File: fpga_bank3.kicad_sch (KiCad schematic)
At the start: 1 part, among them U2 XC7A50T-FGG484

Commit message: Schematic finished, starting layout
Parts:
- added C79, C80, C81, C82, C83, C84, C86, C87, C88, C89, C90, C91: 100n, Capacitor_SMD:C_0402_1005Metric_Pad0.74x0.62mm_HandSolder, symbol Device:C_Small
- added C85, C92: 4.7u, Capacitor_SMD:C_0402_1005Metric_Pad0.74x0.62mm_HandSolder, symbol Device:C_Small
- added R33: 3.9k, Resistor_SMD:R_0402_1005Metric_Pad0.72x0.64mm_HandSolder, symbol Device:R_Small
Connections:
- net +3V3: now also C79.2, C80.2, C81.2, C82.2, C83.2, C84.2, C85.2, C86.2, C87.2, C88.2, C89.2, C90.2, C91.2, C92.2
- net PI_UART_TX: now reaches U2.B1 (IO_L1P_T0_AD4P_35)
- net PI_UART_RX: now reaches U2.C2 (IO_L2P_T0_AD12P_35)
- net PCIE_DET_WAKE: now reaches U2.E2 (IO_L4P_T0_35)
- net at U2.F3 (IO_L6P_T0_35): now also R33.1
- net PCIE_CLKREQ_N: now reaches U2.G1 (IO_L5P_T0_AD13P_35)
- net SPI1_SCK: now reaches U2.G4 (IO_L12N_T1_MRCC_35)
- net REFCLK: now reaches U2.H4 (IO_L12P_T1_MRCC_35)
- net PCIE_RST_B: now reaches U2.J1 (IO_L7N_T1_AD6N_35)
- net SPI1_MOSI: now reaches U2.J4 (IO_L13N_T2_MRCC_35)
- net PI_GPIO13: now reaches U2.J6 (IO_L17N_T2_35)
- net SPI1_CE1: now reaches U2.K3 (IO_L14N_T2_SRCC_35)
- net SPI1_MISO: now reaches U2.K4 (IO_L13P_T2_MRCC_35)
- net PI_GPIO12: now reaches U2.K6 (IO_L17P_T2_35)
- net PI_GPIO4: now reaches U2.L1 (IO_L15N_T2_DQS_35)
- net SPI1_CE0: now reaches U2.L3 (IO_L14P_T2_SRCC_35)
- net PI_GPIO26: now reaches U2.L4 (IO_L18N_T2_35)
- net PI_GPIO22: now reaches U2.L5 (IO_L18P_T2_35)
- net SPI1_CE2: now reaches U2.M1 (IO_L15P_T2_DQS_35)
- net PI_GPIO6: now reaches U2.M2 (IO_L16N_T2_35)
- net PI_GPIO5: now reaches U2.M3 (IO_L16P_T2_35)
- net PI_GPIO27: now reaches U2.N4 (IO_L19P_T3_35)
- new net GND: C79.1, C80.1, C81.1, C82.1, C83.1, C84.1, C85.1, C86.1, C87.1, C88.1, C89.1, C90.1, C91.1, C92.1
- new net PCIE_PWR_EN: R33.2
- no-connect marks 0 -> 79
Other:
- note added: "-->"
- note added: "<--"
- title: FPGA Bank 34 & 35 -> FPGA Power
- moved on the sheet: U2C

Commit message: Updated titleblock texts
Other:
- title: FPGA Power -> FPGA Banks 34 & 35
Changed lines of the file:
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@@
   (paper "A4")
   (title_block
-    (title "FPGA Power")
-    (date "2024-02-11")
+    (title "FPGA Banks 34 & 35")
+    (date "2024-02-14")
     (rev "0.1")
     (company "George Smart, M1GEO")

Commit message: Started routing. More to go
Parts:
- removed R33: 3.9k, Resistor_SMD:R_0402_1005Metric_Pad0.72x0.64mm_HandSolder, symbol Device:R_Small
- added R17: 3.9k, Resistor_SMD:R_0402_1005Metric_Pad0.72x0.64mm_HandSolder, symbol Device:R_Small
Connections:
- net PCIE_CLKREQ_N: now also U2.J1 (IO_L7N_T1_AD6N_35); no longer U2.G1 (IO_L5P_T0_AD13P_35)
- net PCIE_DET_WAKE: now also U2.K1 (IO_L7P_T1_AD6P_35); no longer U2.E2 (IO_L4P_T0_35)
- net PCIE_PWR_EN: now also R17.2
- net PCIE_RST_B: now also U2.G1 (IO_L5P_T0_AD13P_35); no longer U2.J1 (IO_L7N_T1_AD6N_35)
- net PI_GPIO22: now also U2.F3 (IO_L6P_T0_35); no longer U2.L5 (IO_L18P_T2_35)
- net PI_GPIO27: now also U2.B2 (IO_L2N_T0_AD12N_35); no longer U2.N4 (IO_L19P_T3_35)
- net PI_GPIO4: now also U2.F1 (IO_L5N_T0_AD13N_35); no longer U2.L1 (IO_L15N_T2_DQS_35)
- net PI_UART_RX: now also U2.E1 (IO_L3P_T0_DQS_AD5P_35); no longer U2.C2 (IO_L2P_T0_AD12P_35)
- net PI_UART_TX: now also U2.L1 (IO_L15N_T2_DQS_35); no longer U2.B1 (IO_L1P_T0_AD4P_35)
- net PI_GPIO17: now reaches U2.D1 (IO_L3N_T0_DQS_AD5N_35)
- net PI_GPIO2: now reaches U2.P1 (IO_L20N_T3_35)
- net at U2.R1 (IO_L20P_T3_35): now also R17.1
- net PI_GPIO12: no longer names the net of U2.K6 (IO_L17P_T2_35)
- net PI_GPIO13: no longer names the net of U2.J6 (IO_L17N_T2_35)
- net PI_GPIO26: no longer names the net of U2.L4 (IO_L18N_T2_35)
- net PI_GPIO5: no longer names the net of U2.M3 (IO_L16P_T2_35)
- net PI_GPIO6: no longer names the net of U2.M2 (IO_L16N_T2_35)
- net REFCLK: no longer names the net of U2.H4 (IO_L12P_T1_MRCC_35)
- net SPI1_CE0: no longer names the net of U2.L3 (IO_L14P_T2_SRCC_35)
- net SPI1_CE1: no longer names the net of U2.K3 (IO_L14N_T2_SRCC_35)
- net SPI1_CE2 renamed PI_GPIO3
- net SPI1_MISO: no longer names the net of U2.K4 (IO_L13P_T2_MRCC_35)
- net SPI1_MOSI: no longer names the net of U2.J4 (IO_L13N_T2_MRCC_35)
- net SPI1_SCK: no longer names the net of U2.G4 (IO_L12N_T1_MRCC_35)
- new net PI_GPIO18: U2.B1 (IO_L1P_T0_AD4P_35)
- no-connect marks 79 -> 84
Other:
- moved on the sheet: C79, C80, C81, C82, C83, C84, C85, C86, C87, C88, C89, C90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

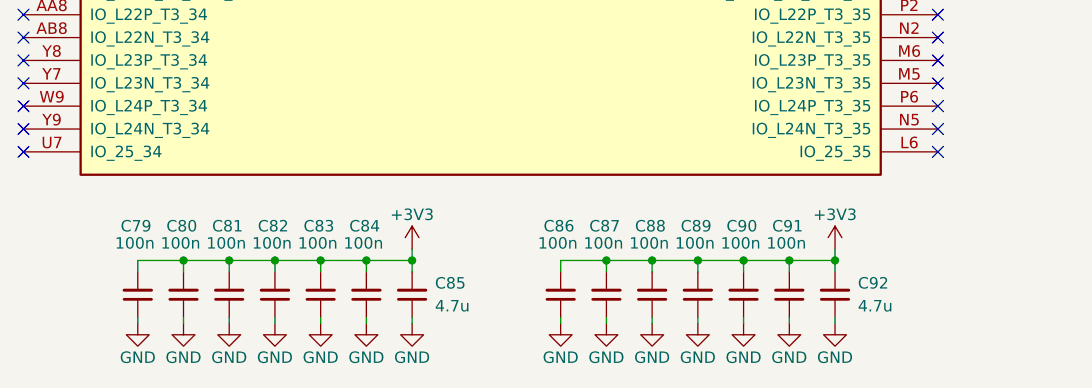
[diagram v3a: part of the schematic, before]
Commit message: Updated decoupling. Need to work out larger planes and fills.
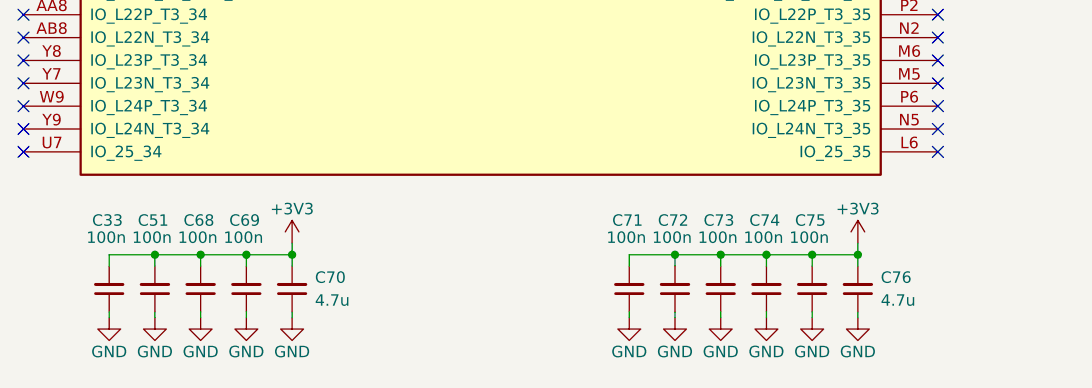
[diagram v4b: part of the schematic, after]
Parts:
- removed C79, C80, C81, C82, C83, C84, C86, C87, C88, C89, C90, C91: 100n, Capacitor_SMD:C_0402_1005Metric_Pad0.74x0.62mm_HandSolder, symbol Device:C_Small
- removed C85, C92: 4.7u, Capacitor_SMD:C_0402_1005Metric_Pad0.74x0.62mm_HandSolder, symbol Device:C_Small
- added C33, C51, C68, C69, C71, C72, C73, C74, C75: 100n, Capacitor_SMD:C_0402_1005Metric_Pad0.74x0.62mm_HandSolder, symbol Device:C_Small
- added C70, C76: 4.7u, Capacitor_SMD:C_0402_1005Metric_Pad0.74x0.62mm_HandSolder, symbol Device:C_Small
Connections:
- net +3V3: now also C33.2, C51.2, C68.2, C69.2, C70.2, C71.2, C72.2, C73.2, C74.2, C75.2, C76.2
- net GND: now also C33.1, C51.1, C68.1, C69.1, C70.1, C71.1, C72.1, C73.1, C74.1, C75.1, C76.1

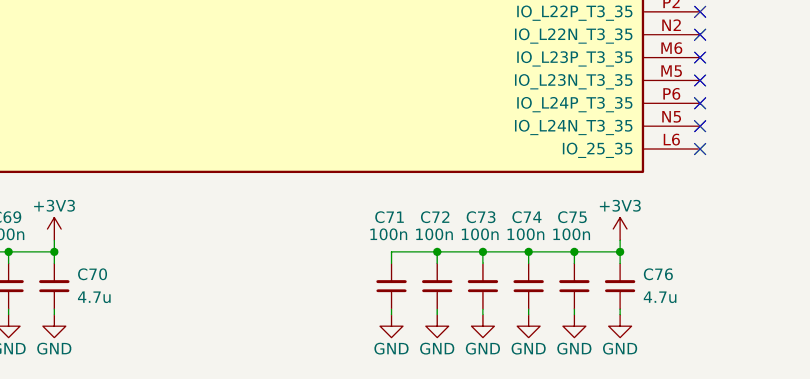
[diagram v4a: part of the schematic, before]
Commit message: Routing finished; Need to battle through the DRCs now. There's a few!
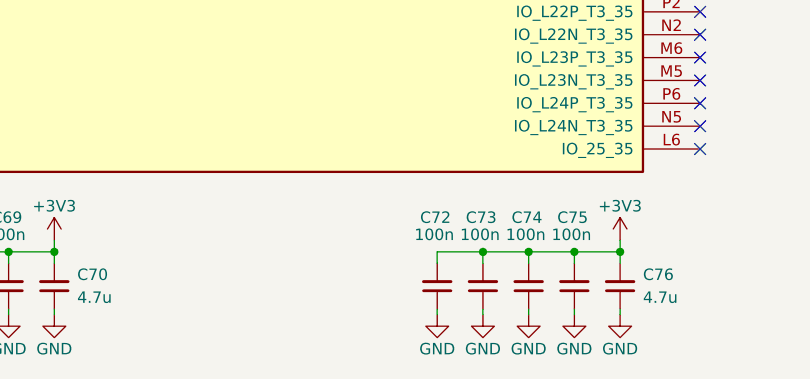
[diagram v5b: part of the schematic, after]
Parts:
- removed C71: 100n, Capacitor_SMD:C_0402_1005Metric_Pad0.74x0.62mm_HandSolder, symbol Device:C_Small
- R17: footprint Resistor_SMD:R_0402_1005Metric_Pad0.72x0.64mm_HandSolder -> Resistor_SMD:R_0402_1005Metric
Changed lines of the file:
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@@
   (junction (at 87.63 181.61) (diameter 0) (color 0 0 0 0)
-  )
-  (junction (at 135.255 181.61) (diameter 0) (color 0 0 0 0)
   )
   (junction (at 154.305 22.86) (diameter 0) (color 0 0 0 0)
@@
     (stroke (width 0) (type default))
   )
-  (wire (pts (xy 130.175 187.96) (xy 130.175 188.595))
-    (stroke (width 0) (type default))
-  )
   (wire (pts (xy 140.335 187.96) (xy 140.335 188.595))
     (stroke (width 0) (type default))
@@
     (stroke (width 0) (type default))
   )
-  (wire (pts (xy 130.175 181.61) (xy 135.255 181.61))
-    (stroke (width 0) (type default))
-  )
   (wire (pts (xy 80.645 25.4) (xy 80.645 22.86))
     (stroke (width 0) (type default))
@@
   )
   (wire (pts (xy 141.605 22.86) (xy 141.605 25.4))
-    (stroke (width 0) (type default))
-  )
-  (wire (pts (xy 130.175 182.88) (xy 130.175 181.61))
     (stroke (width 0) (type default))
   )
@@
       (effects (font (size 1.27 1.27)))
     )
-    (property "Footprint" "Resistor_SMD:R_0402_1005Metric_Pad0.72x0.64mm_HandSolder" (at 170.815 144.78 0)
+    (property "Footprint" "Resistor_SMD:R_0402_1005Metric" (at 170.815 144.78 0)
       (effects (font (size 1.27 1.27)) hide)
     )
@@
     )
   )
-  (symbol (lib_id "Device:C_Small") (at 130.175 185.42 180) (unit 1)
-    (in_bom yes) (on_board yes) (dnp no)
-    (property "Reference" "C71" (at 128.27 177.8 0)
-      (effects (font (size 1.27 1.27)) (justify right))
-    )
-    (property "Value" "100n" (at 127.635 179.705 0)
-      (effects (font (size 1.27 1.27)) (justify right))
-    )
-    (property "Footprint" "Capacitor_SMD:C_0402_1005Metric_Pad0.74x0.62mm_HandSolder" (at 130.175 185.42 0)
-      (effects (font (size 1.27 1.27)) hide)
-    )
-    (property "Datasheet" "https://datasheet.lcsc.com/lcsc/2304140030_Samsung-Electro-Mechanics-CL05B104KO5NNNC_C1525.pdf" (at 130.175 185.42 0)
-      (effects (font (size 1.27 1.27)) hide)
-    )
-    (property "LCSC" "C1525" (at 130.175 185.42 90)
-      (effects (font (size 1.27 1.27)) hide)
-    )
-    (pin "2")
-    (pin "1")
-    (instances
-      (project "Pi5-Artix50T-Hat"
-        (path "/e63e39d7-6ac0-4ffd-8aa3-1841a4541b55/58f29d61-b732-4149-afb6-3ea37966fd1b/478e6a6c-f816-4e6b-8386-2aa7bc333436"
-          (reference "C71") (unit 1)
-        )
-      )
-    )
-  )
   (symbol (lib_id "power:GND") (at 92.71 188.595 0) (unit 1)
     (in_bom yes) (on_board yes) (dnp no)
@@
         )
       )
-    )
-  )
-  (symbol (lib_id "power:GND") (at 130.175 188.595 0) (unit 1)
-    (in_bom yes) (on_board yes) (dnp no)
-    (property "Reference" "#PWR0115" (at 130.175 194.945 0)
-      (effects (font (size 1.27 1.27)) hide)
-    )
-    (property "Value" "GND" (at 130.175 192.405 0)
-      (effects (font (size 1.27 1.27)))
-    )
-    (property "Footprint" "" (at 130.175 188.595 0)
-      (effects (font (size 1.27 1.27)) hide)
-    )
-    (property "Datasheet" "" (at 130.175 188.595 0)
-      (effects (font (size 1.27 1.27)) hide)
-    )
-    (pin "1")
-    (instances
-      (project "Pi5-Artix50T-Hat"
-        (path "/e63e39d7-6ac0-4ffd-8aa3-1841a4541b55/58f29d61-b732-4149-afb6-3ea37966fd1b/478e6a6c-f816-4e6b-8386-2aa7bc333436"
-          (reference "#PWR0115") (unit 1)
-        )
-      )

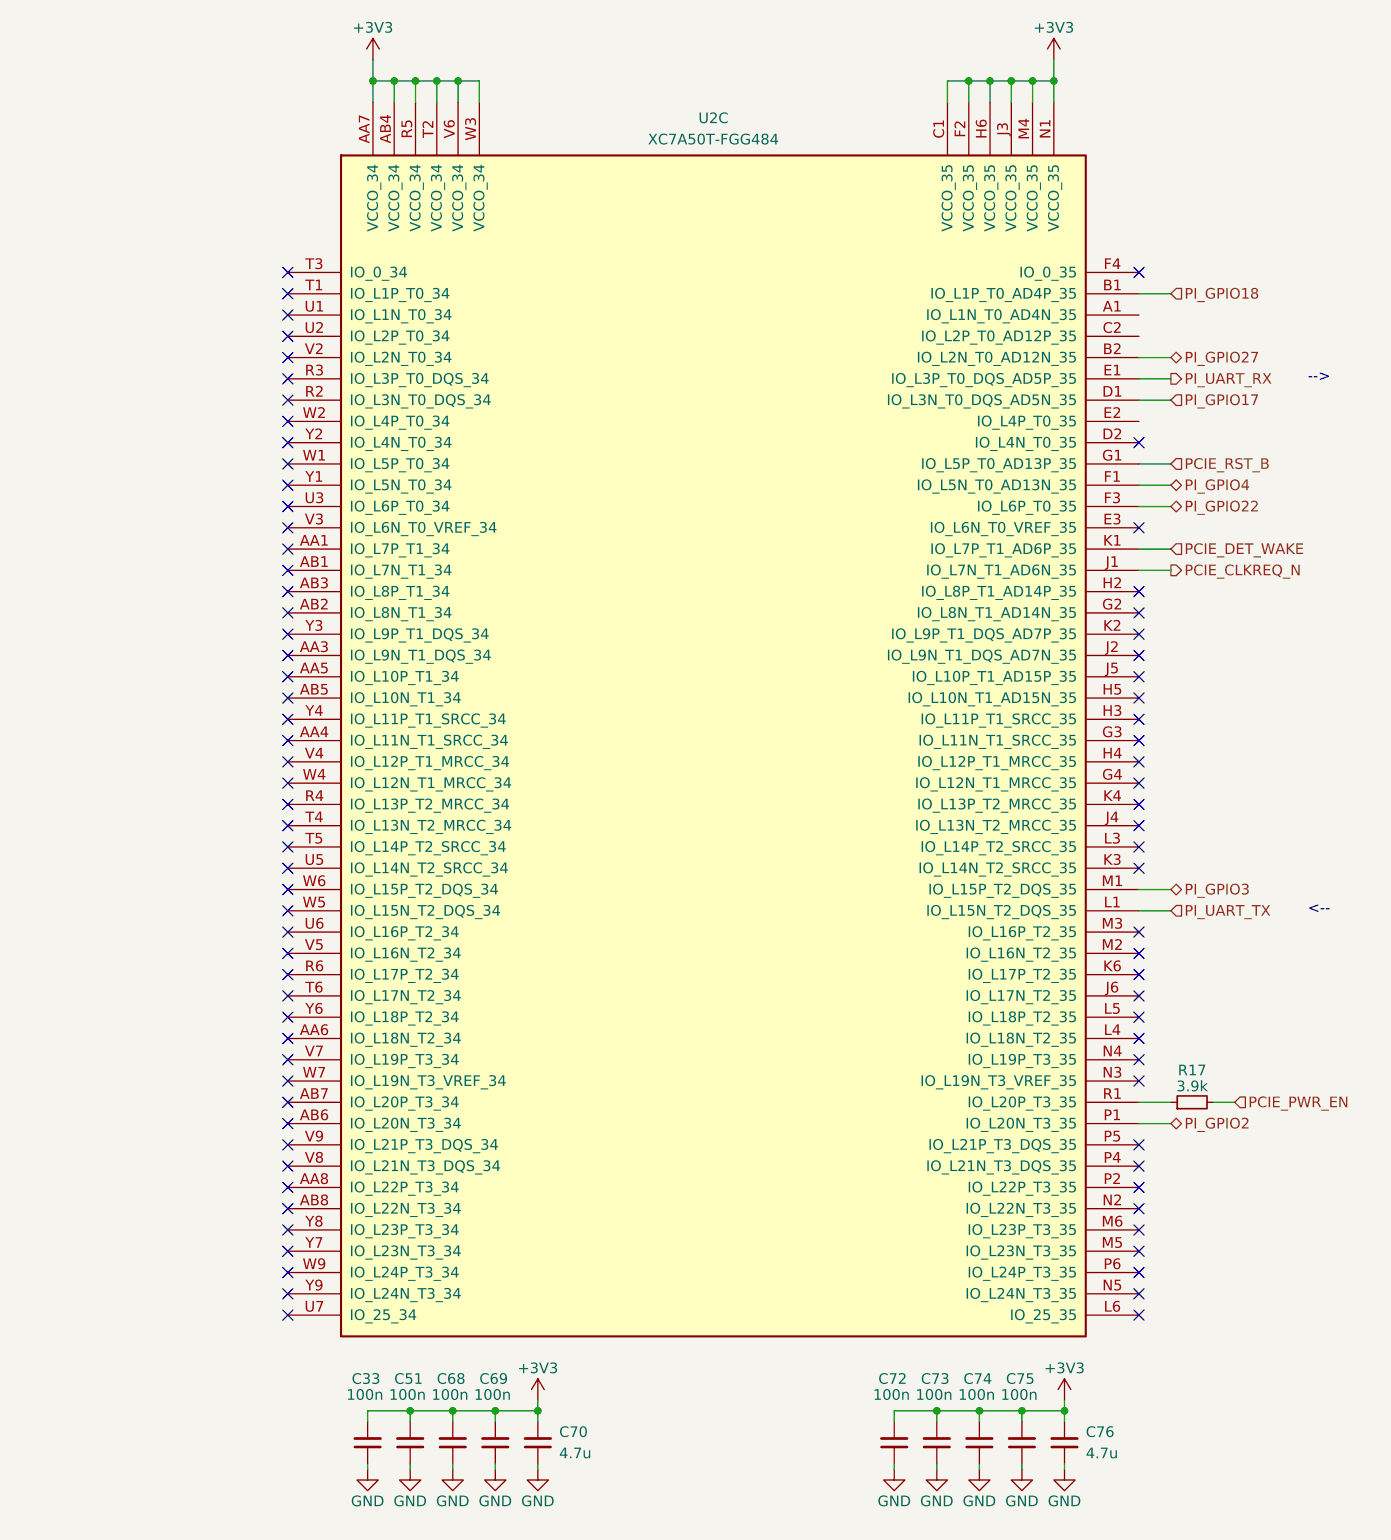
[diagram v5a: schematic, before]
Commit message: Ordered boards from JLCPCB for V1
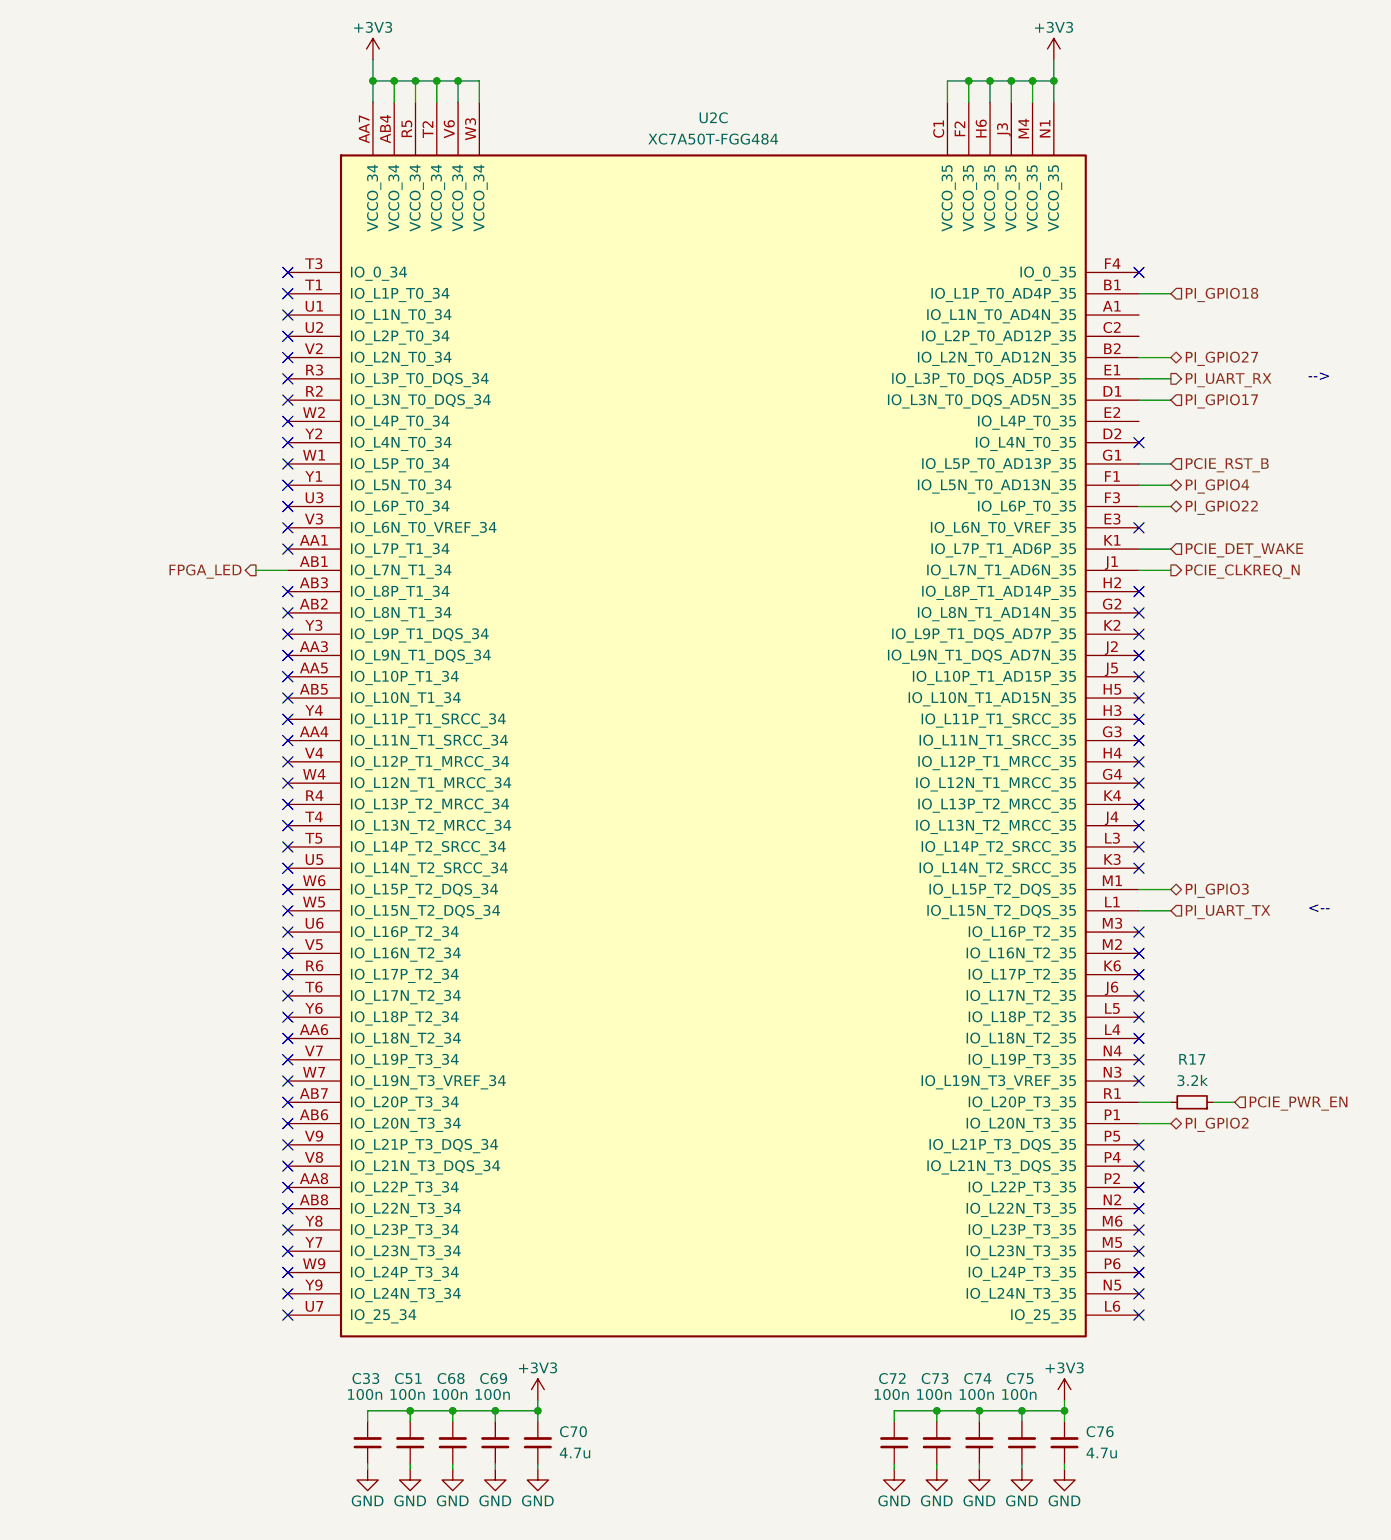
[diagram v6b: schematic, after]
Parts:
- C33, C51, C68, C69, C70, C72, C73, C74, C75, C76: footprint Capacitor_SMD:C_0402_1005Metric_Pad0.74x0.62mm_HandSolder -> Capacitor_SMD:C_0402_1005Metric
- R17: value 3.9k -> 3.2k; LCSC (none) -> C853935
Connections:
- net PCIE_PWR_EN: now also R17.1; no longer R17.2
- net FPGA_LED: now reaches U2.AB1 (IO_L7N_T1_34)
- net at U2.R1 (IO_L20P_T3_35): now also R17.2; no longer R17.1
- no-connect marks 84 -> 83
